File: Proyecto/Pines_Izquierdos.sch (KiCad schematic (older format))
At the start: 2 parts

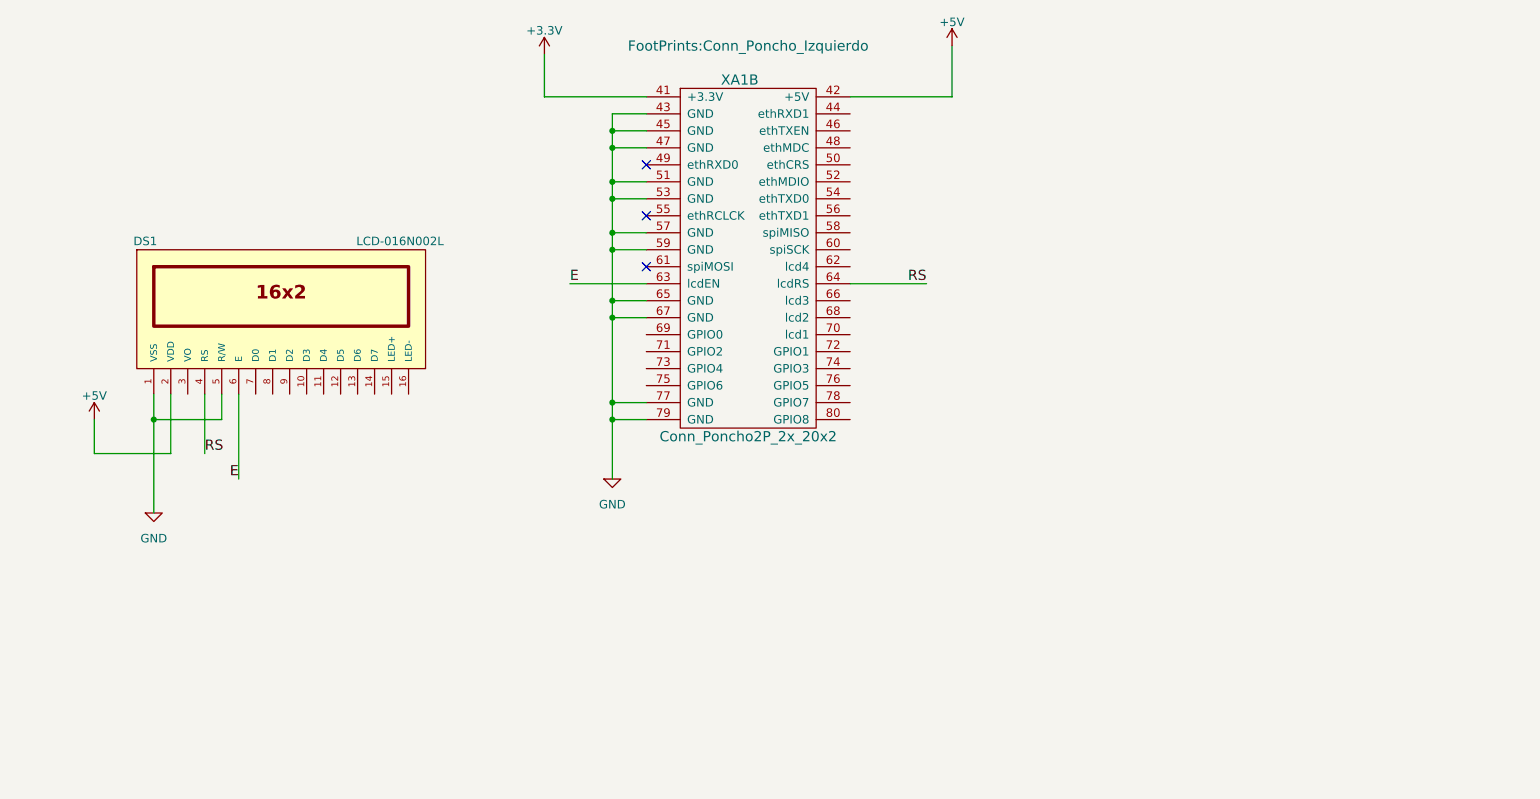
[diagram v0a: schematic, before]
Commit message: Actualización de documentación y esquemáticos.
Se actualizaron los archivos de datos y caracteristicas de los displays
y se adelantó a un 90% el diseño de los esquemáticos de KiCad.
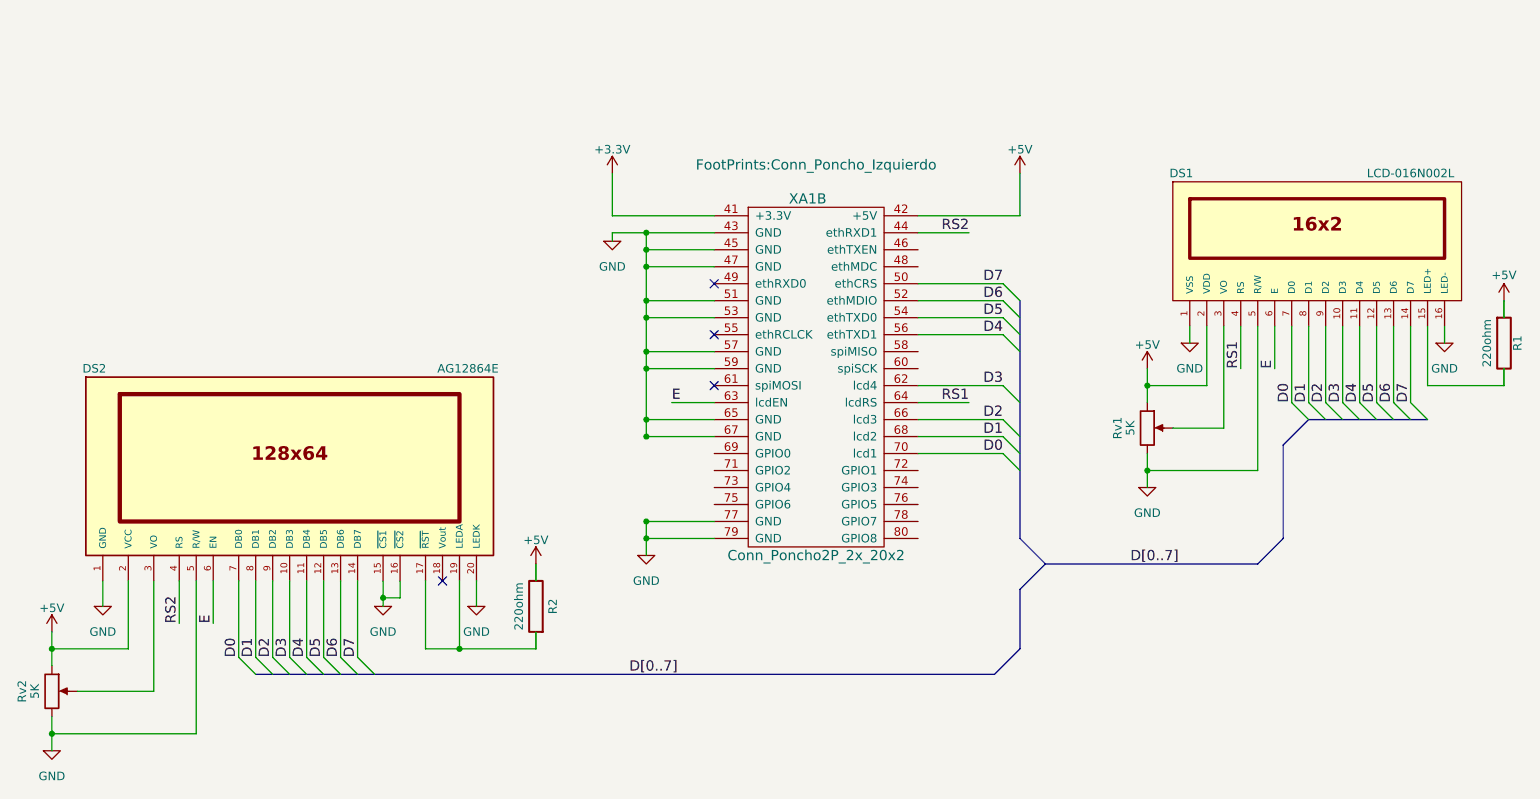
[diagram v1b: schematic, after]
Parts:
- added DS2: AG12864E, AG12864E, symbol AG12864E
- added R1, R2: 220ohm, symbol R
- added Rv1, Rv2: 5K, symbol POT
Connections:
- net labels added: D0, D1, D2, D3, D4, D5, D6, D7, D[0..7], RS1, RS2
- net labels removed: RS
- wire segments 26 -> 81
- no-connect marks 3 -> 4
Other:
- moved on the sheet: DS1, XA1B

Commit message: Avance de FootPrints
Se terminó diseño de esquemáticos en ojas Jerárquicas; se avanzó a un
70% en las referencias de FootPrint, y se actualizaron hojas de datos de
la Matriz de LEDs 8x8.
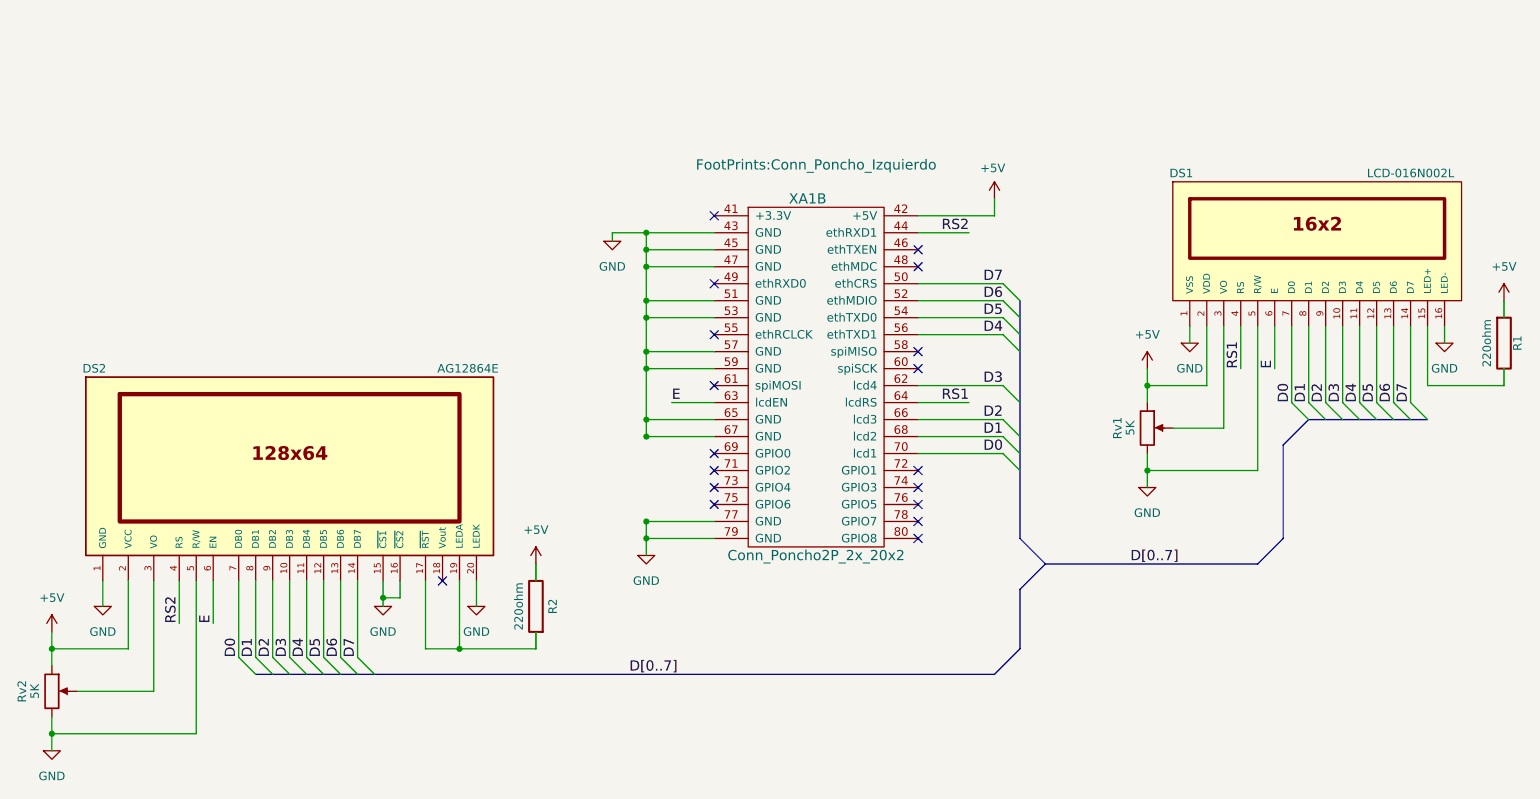
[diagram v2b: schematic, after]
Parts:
- DS1: footprint WC1602A -> FootPrints:LCD-016N002L
- DS2: footprint AG12864E -> FootPrints:AG12864E
- R1, R2: footprint (none) -> FootPrints:R_0805_HandSoldering
- Rv1, Rv2: footprint (none) -> FootPrints:POT_SMD
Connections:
- net labels removed: +3.3V
- wire segments 81 -> 79
- no-connect marks 4 -> 18
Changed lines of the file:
@@
 EESchema Schematic File Version 2
-LIBS:8x8led-cache
 LIBS:power
 LIBS:device
 LIBS:display
 LIBS:Poncho_Esqueleto
-LIBS:MAX7219
 LIBS:Poncho_Educativo_v2.0-cache
 EELAYER 25 0
@@
 $Descr A4 11693 8268
 encoding utf-8
-Sheet 2 3
+Sheet 3 3
 Title "Esquemático de conexión para pines Izquierdos."
 Date "2017-05-22"
@@
 P 7900 3850
 AR Path="/59239964" Ref="#PWR?"  Part="1"
-AR Path="/591BB8C8/59239964" Ref="#PWR?"  Part="1"
-F 0 "#PWR?" H 7900 3600 50  0001 C CNN
+AR Path="/591BB8C8/59239964" Ref="#PWR09"  Part="1"
+F 0 "#PWR09" H 7900 3600 50  0001 C CNN
 F 1 "GND" H 7900 3700 50  0000 C CNN
 F 2 "" H 7900 3850 50  0001 C CNN
@@
 P 4950 4250
 AR Path="/5923997C" Ref="#PWR?"  Part="1"
-AR Path="/591BB8C8/5923997C" Ref="#PWR?"  Part="1"
-F 0 "#PWR?" H 4950 4000 50  0001 C CNN
+AR Path="/591BB8C8/5923997C" Ref="#PWR010"  Part="1"
+F 0 "#PWR010" H 4950 4000 50  0001 C CNN
 F 1 "GND" H 4950 4100 50  0000 C CNN
 F 2 "" H 4950 4250 50  0001 C CNN
@@
 NoConn ~ 5350 2950
 NoConn ~ 5350 3250
-$Comp
-L +3.3V #PWR?
-U 1 1 59239B46
-P 4750 2000
-F 0 "#PWR?" H 4750 1850 50  0001 C CNN
-F 1 "+3.3V" H 4750 2140 50  0000 C CNN
-F 2 "" H 4750 2000 50  0001 C CNN
-F 3 "" H 4750 2000 50  0001 C CNN
-	1    4750 2000
-	1    0    0    -1
-$EndComp
-$Comp
-L +5V #PWR?
-U 1 1 59239B93
-P 7150 2000
-F 0 "#PWR?" H 7150 1850 50  0001 C CNN
-F 1 "+5V" H 7150 2140 50  0000 C CNN
-F 2 "" H 7150 2000 50  0001 C CNN
-F 3 "" H 7150 2000 50  0001 C CNN
-	1    7150 2000
-	1    0    0    -1
-$EndComp
 Text Label 5100 3350 0    60   ~ 0
 E
@@
 E
 $Comp
-L +5V #PWR?
+L +5V #PWR011
 U 1 1 59239CAA
 P 7900 3150
-F 0 "#PWR?" H 7900 3000 50  0001 C CNN
-F 1 "+5V" H 7900 3290 50  0000 C CNN
+F 0 "#PWR011" H 7900 3000 50  0001 C CNN
+F 1 "+5V" H 7900 3350 50  0000 C CNN
 F 2 "" H 7900 3150 50  0001 C CNN
 F 3 "" H 7900 3150 50  0001 C CNN
@@
 F 0 "Rv1" V 7725 3500 50  0000 C CNN
 F 1 "5K" V 7800 3500 50  0000 C CNN
-F 2 "" H 7900 3500 50  0001 C CNN
+F 2 "FootPrints:POT_SMD" H 7900 3500 50  0001 C CNN
 F 3 "" H 7900 3500 50  0001 C CNN
 	1    7900 3500
@@
 F 0 "DS1" H 8100 2800 50  0000 C CNN
 F 1 "LCD-016N002L" H 9450 2800 50  0000 C CNN
-F 2 "WC1602A" H 8900 2350 50  0001 C CIN
+F 2 "FootPrints:LCD-016N002L" H 8900 2350 50  0001 C CIN
 F 3 "" H 8900 2400 50  0001 C CNN
 	1    8900 2400
@@
 P 8150 3000
 AR Path="/5924DD46" Ref="#PWR?"  Part="1"
-AR Path="/591BB8C8/5924DD46" Ref="#PWR?"  Part="1"
-F 0 "#PWR?" H 8150 2750 50  0001 C CNN
+AR Path="/591BB8C8/5924DD46" Ref="#PWR012"  Part="1"
+F 0 "#PWR012" H 8150 2750 50  0001 C CNN
 F 1 "GND" H 8150 2850 50  0000 C CNN
 F 2 "" H 8150 3000 50  0001 C CNN
@@
 D[0..7]
 $Comp
-L +5V #PWR?
+L +5V #PWR013
 U 1 1 5924EC76
 P 10000 2750
-F 0 "#PWR?" H 10000 2600 50  0001 C CNN
-F 1 "+5V" H 10000 2900 50  0000 C CNN
+F 0 "#PWR013" H 10000 2600 50  0001 C CNN
+F 1 "+5V" H 10000 2950 50  0000 C CNN
 F 2 "" H 10000 2750 50  0001 C CNN
 F 3 "" H 10000 2750 50  0001 C CNN
@@
 P 9650 3000
 AR Path="/5924EC90" Ref="#PWR?"  Part="1"
-AR Path="/591BB8C8/5924EC90" Ref="#PWR?"  Part="1"
-F 0 "#PWR?" H 9650 2750 50  0001 C CNN
+AR Path="/591BB8C8/5924EC90" Ref="#PWR014"  Part="1"
+F 0 "#PWR014" H 9650 2750 50  0001 C CNN
 F 1 "GND" H 9650 2850 50  0000 C CNN
 F 2 "" H 9650 3000 50  0001 C CNN
@@
 P 4750 2400
 AR Path="/5924F240" Ref="#PWR?"  Part="1"
-AR Path="/591BB8C8/5924F240" Ref="#PWR?"  Part="1"
-F 0 "#PWR?" H 4750 2150 50  0001 C CNN
+AR Path="/591BB8C8/5924F240" Ref="#PWR015"  Part="1"
+F 0 "#PWR015" H 4750 2150 50  0001 C CNN
 F 1 "GND" H 4750 2250 50  0000 C CNN
 F 2 "" H 4750 2400 50  0001 C CNN
@@
 F 0 "DS2" H 1700 4450 50  0000 C CNN
 F 1 "AG12864E" H 3900 4450 50  0000 C CNN
-F 2 "AG12864E" H 2850 3600 50  0001 C CIN
-F 3 "" H 2850 3800 50  0001 C CNN
+F 2 "FootPrints:AG12864E" H 2850 3600 50  0001 C CIN
+F 3 "MGL5128 128x64 Graphic LCD Module - User Manual.pdf" H 2850 3800 50  0001 C CNN
 	1    2850 3800
 	1    0    0    -1
@@
 P 1750 4550
 AR Path="/59262698" Ref="#PWR?"  Part="1"
-AR Path="/591BB8C8/59262698" Ref="#PWR?"  Part="1"
-F 0 "#PWR?" H 1750 4300 50  0001 C CNN
+AR Path="/591BB8C8/59262698" Ref="#PWR016"  Part="1"
+F 0 "#PWR016" H 1750 4300 50  0001 C CNN
 F 1 "GND" H 1750 4400 50  0000 C CNN
 F 2 "" H 1750 4550 50  0001 C CNN
@@
 F 0 "Rv2" V 1275 5050 50  0000 C CNN
 F 1 "5K" V 1350 5050 50  0000 C CNN
-F 2 "" H 1450 5050 50  0001 C CNN
+F 2 "FootPrints:POT_SMD" H 1450 5050 50  0001 C CNN
 F 3 "" H 1450 5050 50  0001 C CNN
 	1    1450 5050
@@
 $EndComp
 $Comp
-L +5V #PWR?
+L +5V #PWR017
 U 1 1 5926296A
 P 1450 4700
-F 0 "#PWR?" H 1450 4550 50  0001 C CNN
-F 1 "+5V" H 1450 4840 50  0000 C CNN
+F 0 "#PWR017" H 1450 4550 50  0001 C CNN
+F 1 "+5V" H 1450 4900 50  0000 C CNN
 F 2 "" H 1450 4700 50  0001 C CNN
 F 3 "" H 1450 4700 50  0001 C CNN
@@
 P 1450 5400
 AR Path="/59262A0A" Ref="#PWR?"  Part="1"
-AR Path="/591BB8C8/59262A0A" Ref="#PWR?"  Part="1"
-F 0 "#PWR?" H 1450 5150 50  0001 C CNN
+AR Path="/591BB8C8/59262A0A" Ref="#PWR018"  Part="1"
+F 0 "#PWR018" H 1450 5150 50  0001 C CNN
 F 1 "GND" H 1450 5250 50  0000 C CNN
 F 2 "" H 1450 5400 50  0001 C CNN
@@
 Connection ~ 4950 2450
 Wire Wire Line
-	5350 2250 4750 2250
-Wire Wire Line
-	4750 2250 4750 2000
-Wire Wire Line
-	6550 2250 7150 2250
-Wire Wire Line
-	7150 2250 7150 2000
-Wire Wire Line
 	8450 2900 8450 3150
 Wire Wire Line
@@
 P 3950 4550
 AR Path="/592653AA" Ref="#PWR?"  Part="1"
-AR Path="/591BB8C8/592653AA" Ref="#PWR?"  Part="1"
-F 0 "#PWR?" H 3950 4300 50  0001 C CNN
+AR Path="/591BB8C8/592653AA" Ref="#PWR019"  Part="1"
+F 0 "#PWR019" H 3950 4300 50  0001 C CNN
 F 1 "GND" H 3950 4400 50  0000 C CNN
 F 2 "" H 3950 4550 50  0001 C CNN
@@
 $EndComp
 $Comp
-L +5V #PWR?
+L +5V #PWR020
 U 1 1 592653C8
 P 4300 4300
-F 0 "#PWR?" H 4300 4150 50  0001 C CNN
-F 1 "+5V" H 4300 4440 50  0000 C CNN
+F 0 "#PWR020" H 4300 4150 50  0001 C CNN
+F 1 "+5V" H 4300 4500 50  0000 C CNN
 F 2 "" H 4300 4300 50  0001 C CNN
 F 3 "" H 4300 4300 50  0001 C CNN
@@
 F 0 "R2" V 4200 4550 50  0000 C CNN
 F 1 "220ohm" V 4400 4550 50  0000 C CNN
-F 2 "" V 4230 4550 50  0001 C CNN
+F 2 "FootPrints:R_0805_HandSoldering" V 4230 4550 50  0001 C CNN
 F 3 "" H 4300 4550 50  0001 C CNN
 	1    4300 4550
@@
 F 0 "R1" V 10080 3000 50  0000 C CNN
 F 1 "220ohm" V 9900 3000 50  0000 C CNN
-F 2 "" V 9930 3000 50  0001 C CNN
+F 2 "FootPrints:R_0805_HandSoldering" V 9930 3000 50  0001 C CNN
 F 3 "" H 10000 3000 50  0001 C CNN
 	1    10000 3000
@@
 P 3400 4550
 AR Path="/5926E76E" Ref="#PWR?"  Part="1"
-AR Path="/591BB8C8/5926E76E" Ref="#PWR?"  Part="1"
-F 0 "#PWR?" H 3400 4300 50  0001 C CNN
+AR Path="/591BB8C8/5926E76E" Ref="#PWR021"  Part="1"
+F 0 "#PWR021" H 3400 4300 50  0001 C CNN
 F 1 "GND" H 3400 4400 50  0000 C CNN
 F 2 "" H 3400 4550 50  0001 C CNN
@@
 	3500 4500 3400 4500
 Connection ~ 3400 4500
+NoConn ~ 5350 3650
+NoConn ~ 5350 3750
+NoConn ~ 5350 3850
+NoConn ~ 5350 3950
+NoConn ~ 6550 4150
+NoConn ~ 6550 4050
+NoConn ~ 6550 3950
+NoConn ~ 6550 3850
+NoConn ~ 6550 3750
+NoConn ~ 6550 3150
+NoConn ~ 6550 3050
+NoConn ~ 6550 2550
+NoConn ~ 6550 2450
+NoConn ~ 5350 2250
+Wire Wire Line
+	7000 2250 6550 2250
+$Comp
+L +5V #PWR022
+U 1 1 592A62F7
+P 7000 2150
+F 0 "#PWR022" H 7000 2000 50  0001 C CNN
+F 1 "+5V" H 6990 2330 50  0000 C CNN
+F 2 "" H 7000 2150 50  0001 C CNN
+F 3 "" H 7000 2150 50  0001 C CNN
+	1    7000 2150
+	1    0    0    -1
+$EndComp
+Wire Wire Line
+	7000 2150 7000 2250
 $EndSCHEMATC
